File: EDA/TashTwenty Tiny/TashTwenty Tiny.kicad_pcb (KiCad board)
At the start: 2 copper layers, 56.6 x 57.7 mm, 31 parts, among them J1 SD_Card, J2 IDC20, J3 Conn_01x02, Q1 BC337, U1 PIC16F1825-IP, U2 74ACT08, U3 MCP1700-3302E_TO92

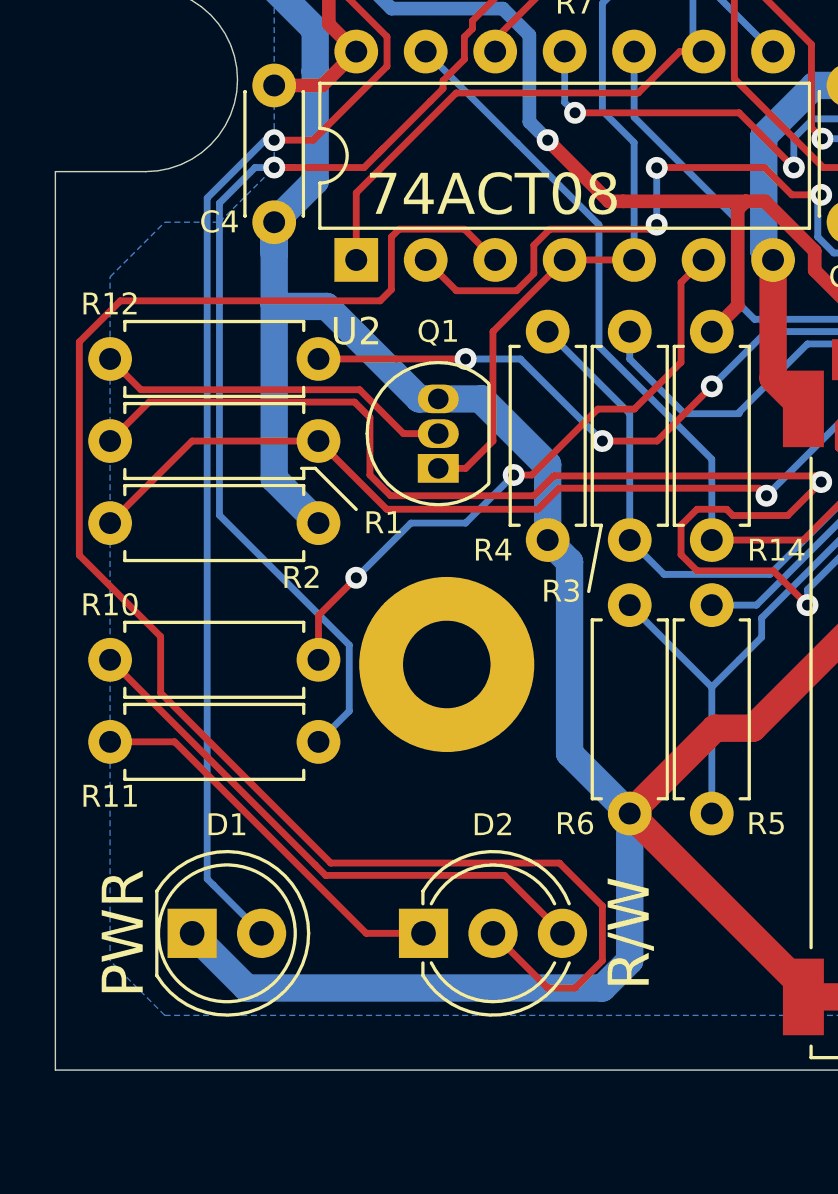
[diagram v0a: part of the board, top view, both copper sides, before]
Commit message: misc tiding (resistors, led, etc…)
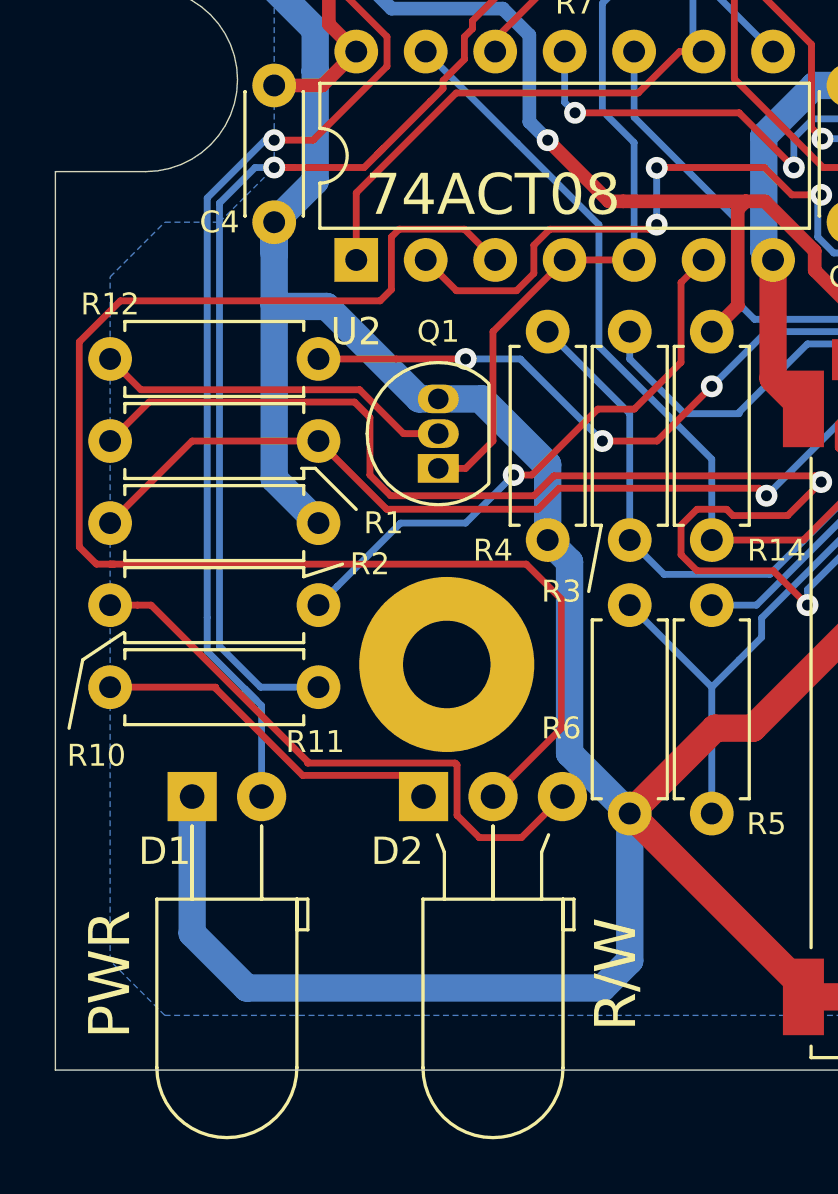
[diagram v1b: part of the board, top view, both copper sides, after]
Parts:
- D1: footprint LED_THT:LED_D5.0mm -> LED_THT:LED_D5.0mm_Horizontal_O3.81mm_Z3.0mm
- D2: footprint LED_THT:LED_D5.0mm-3 -> LED_THT:LED_D5.0mm-3_Horizontal_O3.81mm_Z3.0mm
- moved D1 5.00 mm to (132.0, 117.0)
- moved D2 5.00 mm to (140.5, 117.0)
- moved R10 2.00 mm to (129.0, 110.0)
- moved R11 2.00 mm to (129.0, 113.0)
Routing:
- net Net-(D2-Pad2): track 59.2 -> 52.8 mm
- net Net-(D1-Pad2): track 84.6 -> 80.3 mm
- net GND: track 333.2 -> 336.4 mm
- net Net-(R10-Pad2): track 22.8 -> 21.0 mm, vias 2 -> 1
- net Net-(R11-Pad2): track 55.8 -> 54.1 mm
- net Net-(D2-Pad1): track 14.4 -> 13.1 mm
- net Net-(D2-Pad3): track 20.7 -> 21.8 mm
